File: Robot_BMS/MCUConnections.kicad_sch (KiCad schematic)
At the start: 5 parts, among them J2 39-30-0040, J3 Qwiik1, J4 Qwiik1, J7 Qwiik1, J8 Qwiik1

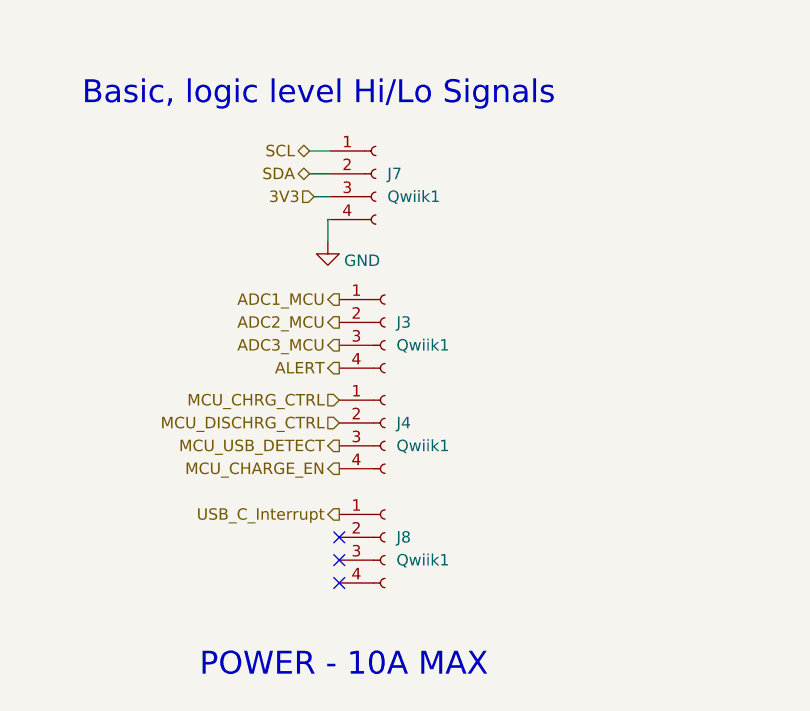
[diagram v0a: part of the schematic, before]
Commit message: creation of seperate 4 layer pcb for individual technical report
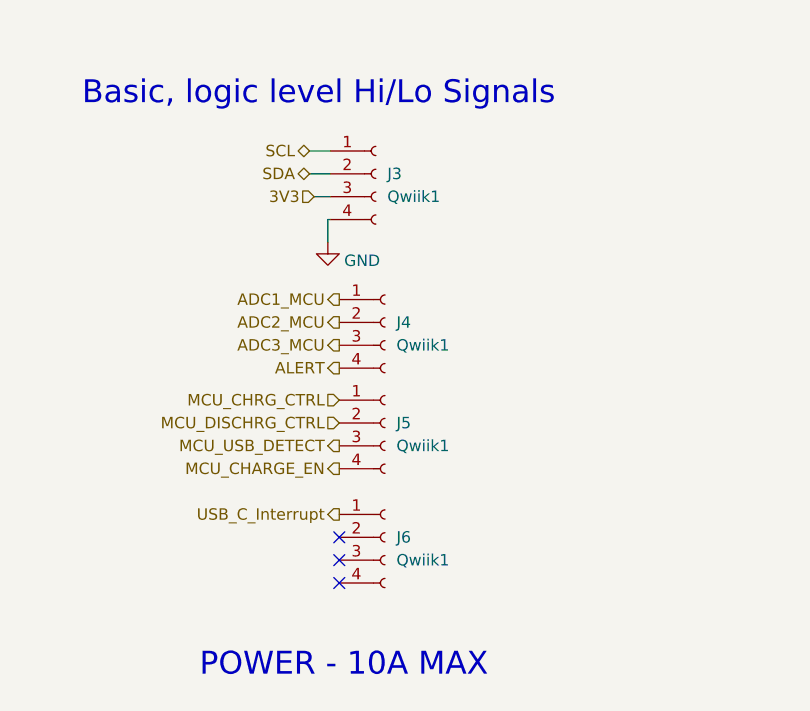
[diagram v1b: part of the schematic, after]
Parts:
- renumbered J7 to J3, J3 to J4, J4 to J5, J8 to J6
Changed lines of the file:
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@@
 		(on_board yes)
 		(dnp no)
-		(property "Reference" "J3"
+		(property "Reference" "J4"
 			(at 152.4 76.9619 0)
 			(effects
@@
 			(project "Robot_BMS"
 				(path "/72551b1c-3d40-4199-8911-e5b015f4abec/f21d0d80-f932-4fe7-82f0-3490cb74f2de"
-					(reference "J3")
+					(reference "J4")
 					(unit 1)
 				)
@@
 		(on_board yes)
 		(dnp no)
-		(property "Reference" "J4"
+		(property "Reference" "J5"
 			(at 152.4 88.1379 0)
 			(effects
@@
 			(project "Robot_BMS"
 				(path "/72551b1c-3d40-4199-8911-e5b015f4abec/f21d0d80-f932-4fe7-82f0-3490cb74f2de"
-					(reference "J4")
+					(reference "J5")
 					(unit 1)
 				)
@@
 		(on_board yes)
 		(dnp no)
-		(property "Reference" "J7"
+		(property "Reference" "J3"
 			(at 151.384 60.4519 0)
 			(effects
@@
 			(project "Robot_BMS"
 				(path "/72551b1c-3d40-4199-8911-e5b015f4abec/f21d0d80-f932-4fe7-82f0-3490cb74f2de"
-					(reference "J7")
+					(reference "J3")
 					(unit 1)
 				)
@@
 		(on_board yes)
 		(dnp no)
-		(property "Reference" "#PWR048"
+		(property "Reference" "#PWR024"
 			(at 144.78 74.422 0)
 			(effects
@@
 			(project "Robot_BMS"
 				(path "/72551b1c-3d40-4199-8911-e5b015f4abec/f21d0d80-f932-4fe7-82f0-3490cb74f2de"
-					(reference "#PWR048")
+					(reference "#PWR024")
 					(unit 1)
 				)
@@
 		(on_board yes)
 		(dnp no)
-		(property "Reference" "#PWR024"
+		(property "Reference" "#PWR025"
 			(at 157.988 139.954 0)
 			(effects
@@
 			(project "Robot_BMS"
 				(path "/72551b1c-3d40-4199-8911-e5b015f4abec/f21d0d80-f932-4fe7-82f0-3490cb74f2de"
-					(reference "#PWR024")
+					(reference "#PWR025")
 					(unit 1)
 				)
@@
 		(on_board yes)
 		(dnp no)
-		(property "Reference" "J8"
+		(property "Reference" "J6"
 			(at 152.4 100.8379 0)
 			(effects
@@
 			(project "Robot_BMS"
 				(path "/72551b1c-3d40-4199-8911-e5b015f4abec/f21d0d80-f932-4fe7-82f0-3490cb74f2de"
-					(reference "J8")
-					(unit 1)
-				)
+					(reference "J6")
+					(unit 1)
+				)

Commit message: halfway throgh battery management pcb layout
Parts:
- added J2: PowerCable, symbol Molex_4pin:Molex_Wire_4pin
- renumbered J2 to J3, J3 to J4, J4 to J5, J5 to J6, J6 to J7
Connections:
- net GND: no longer J3.1, J3.2
- new net TO_LOAD_GND: J3.1, J3.2

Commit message: manufacture ready
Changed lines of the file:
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@@
 (kicad_sch
-	(version 20231120)
+	(version 20250114)
 	(generator "eeschema")
-	(generator_version "8.0")
+	(generator_version "9.0")
 	(paper "A4")
 	(title_block
 		(date "2025-03-13")
+	)
+	(text "All standard Passive\ncomponenets are 0603 imperial"
+		(exclude_from_sim no)
+		(at 214.884 172.72 0)
+		(effects
+			(font
+				(size 2.54 2.54)
+			)
+		)
+	)
+	(text "POWER - 10A MAX"
+		(exclude_from_sim no)
+		(at 146.558 115.062 0)
+		(effects
+			(font
+				(size 2.54 2.54)
+			)
+		)
+	)
+	(text "Basic, logic level Hi/Lo Signals"
+		(exclude_from_sim no)
+		(at 143.764 51.562 0)
+		(effects
+			(font
+				(size 2.54 2.54)
+			)
+		)
+	)
+	(text "link to cable"
+		(exclude_from_sim no)
+		(at 148.59 153.162 0)
+		(effects
+			(font
+				(size 2.54 2.54)
+			)
+			(href "https://uk.farnell.com/molex/45135-0401/cable-assy-4p-rcpt-rcpt-150mm/dp/3862453?MER=BR-MER-MA-RECO-PDP-STM72189")
+		)
+	)
+	(text "Used a molex connector\nhigh current capacity"
+		(exclude_from_sim no)
+		(at 149.86 144.272 0)
+		(effects
+			(font
+				(size 2.54 2.54)
+			)
+		)
+	)
+	(text "Connectors to Interface with other PCB"
+		(exclude_from_sim no)
+		(at 131.826 22.86 0)
+		(effects
+			(font
+				(size 7.62 7.62)
+			)
+		)
 	)
 	(no_connect
@@
 		)
 	)
-	(text "All standard Passive\ncomponenets are 0603 imperial"
-		(exclude_from_sim no)
-		(at 214.884 172.72 0)
-		(effects
-			(font
-				(size 2.54 2.54)
-			)
-		)
-	)
-	(text "POWER - 10A MAX"
-		(exclude_from_sim no)
-		(at 146.558 115.062 0)
-		(effects
-			(font
-				(size 2.54 2.54)
-			)
-		)
-	)
-	(text "Basic, logic level Hi/Lo Signals"
-		(exclude_from_sim no)
-		(at 143.764 51.562 0)
-		(effects
-			(font
-				(size 2.54 2.54)
-			)
-		)
-	)
-	(text "link to cable"
-		(exclude_from_sim no)
-		(at 148.59 153.162 0)
-		(effects
-			(font
-				(size 2.54 2.54)
-			)
-			(href "https://uk.farnell.com/molex/45135-0401/cable-assy-4p-rcpt-rcpt-150mm/dp/3862453?MER=BR-MER-MA-RECO-PDP-STM72189")
-		)
-	)
-	(text "Used a molex connector\nhigh current capacity"
-		(exclude_from_sim no)
-		(at 149.86 144.272 0)
-		(effects
-			(font
-				(size 2.54 2.54)
-			)
-		)
-	)
-	(text "Connectors to Interface with other PCB"
-		(exclude_from_sim no)
-		(at 131.826 22.86 0)
-		(effects
-			(font
-				(size 7.62 7.62)
-			)
-		)
-	)
